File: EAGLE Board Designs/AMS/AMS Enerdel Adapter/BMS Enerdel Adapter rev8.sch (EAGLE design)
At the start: 26 parts, among them J1 CONNECTOR-1_5222_, J10 CONNECTOR-1_5222_, J11 CONNECTOR-1_5222_, J12 CONNECTOR-1_5222_, J13 CONNECTOR-1_5222_, J14 CONNECTOR-1_5222_, J15 CONNECTOR-1_5222_, J16 CONNECTOR-1_5222_, J17 CONNECTOR-1_5222_, J18 CONNECTOR-1_5222_, J19 CONNECTOR-1_5222_, J2 CONNECTOR-1_5222_, J20 CONNECTOR-1_5222_, J21 CONNECTOR-1_5222_, J22 CONNECTOR-1_5222_, J3 CONNECTOR-1_5222_, J4 CONNECTOR-1_5222_, J5 CONNECTOR-1_5222_, J6 CONNECTOR-1_5222_, J7 CONNECTOR-1_5222_, J8 CONNECTOR-1_5222_, J9 CONNECTOR-1_5222_

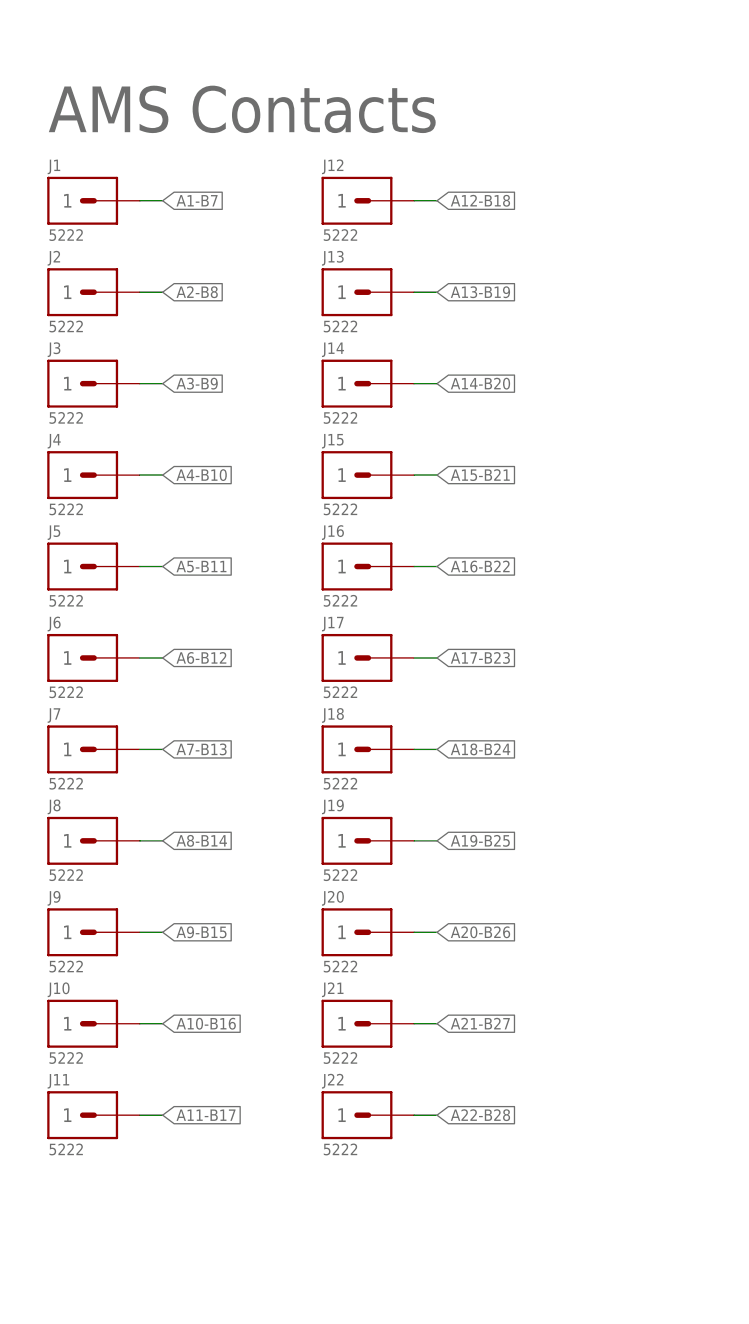
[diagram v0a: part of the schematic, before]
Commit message: added fuses
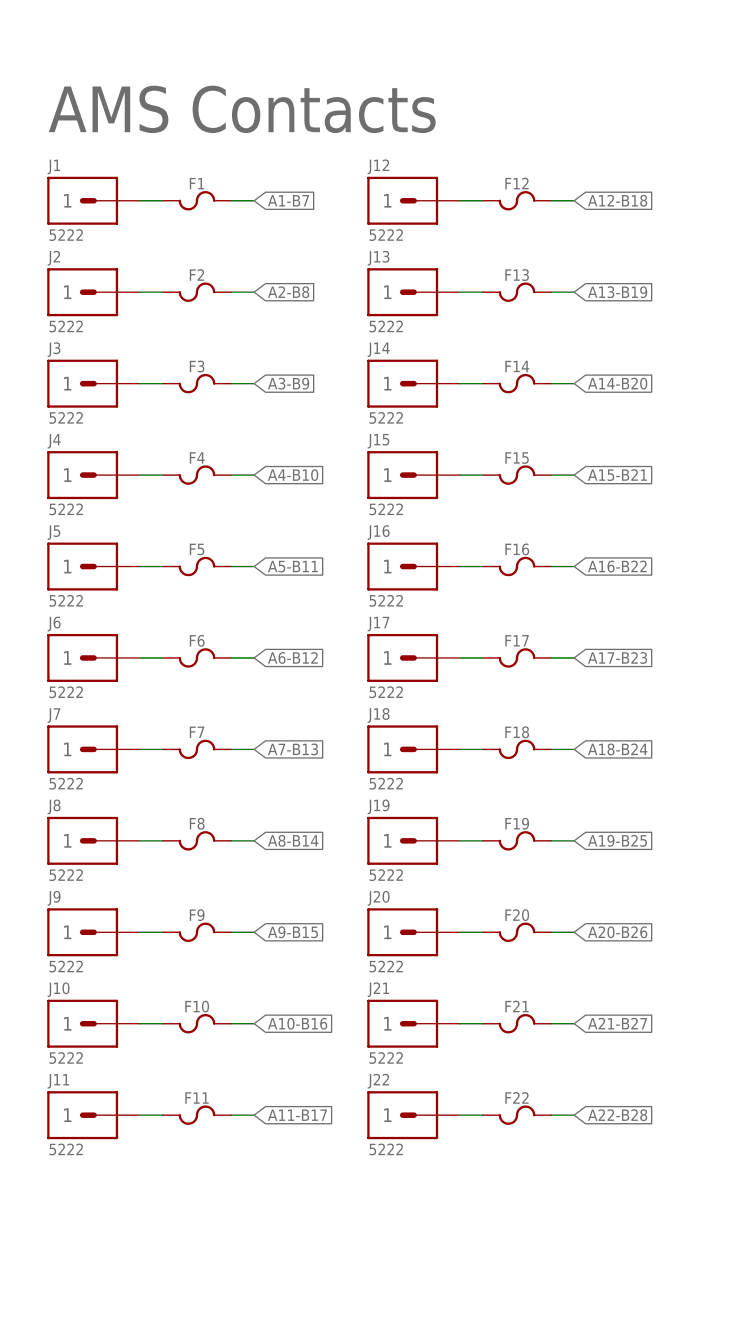
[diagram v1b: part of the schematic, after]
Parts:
- added F1, F10, F11, F12, F13, F14, F15, F16, F17, F18, F19, F2, F20, F21, F22, F3, F4, F5, F6, F7, F8, F9: (no value), HyTechDevices:FUSE_MINIBLADE
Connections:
- new net N$8: F10.1, J10.1
- net A1-B7: now also F1.1, F1.2
- net A10-B16: now also F10.2; no longer J10.1
- net A11-B17: now also F11.1, F11.2
- net A12-B18: now also F12.1, F12.2
- net A13-B19: now also F13.1, F13.2
- net A14-B20: now also F14.1, F14.2
- net A15-B21: now also F15.1, F15.2
- net A16-B22: now also F16.1, F16.2
- net A17-B23: now also F17.1, F17.2
- net A18-B24: now also F18.1, F18.2
- net A19-B25: now also F19.1, F19.2
- net A2-B8: now also F2.1, F2.2
- net A20-B26: now also F20.1, F20.2
- net A21-B27: now also F21.1, F21.2
- net A22-B28: now also F22.1, F22.2
- net A3-B9: now also F3.1, F3.2
- net A4-B10: now also F4.1, F4.2
- net A5-B11: now also F5.1, F5.2
- net A6-B12: now also F6.1, F6.2
- net A7-B13: now also F7.1, F7.2
- net A8-B14: now also F8.1, F8.2
- net A9-B15: now also F9.1, F9.2
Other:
- moved on the sheet: J12, J13, J14, J15, J16, J17, J18, J19, J20, J21, J22

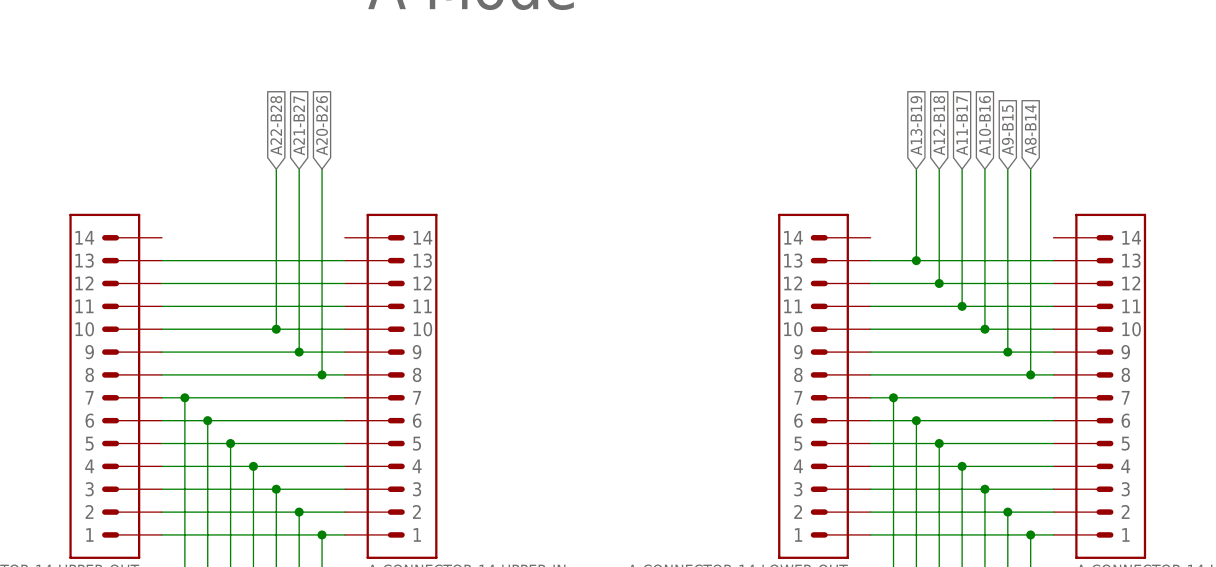
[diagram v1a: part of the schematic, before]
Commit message: routed fuses
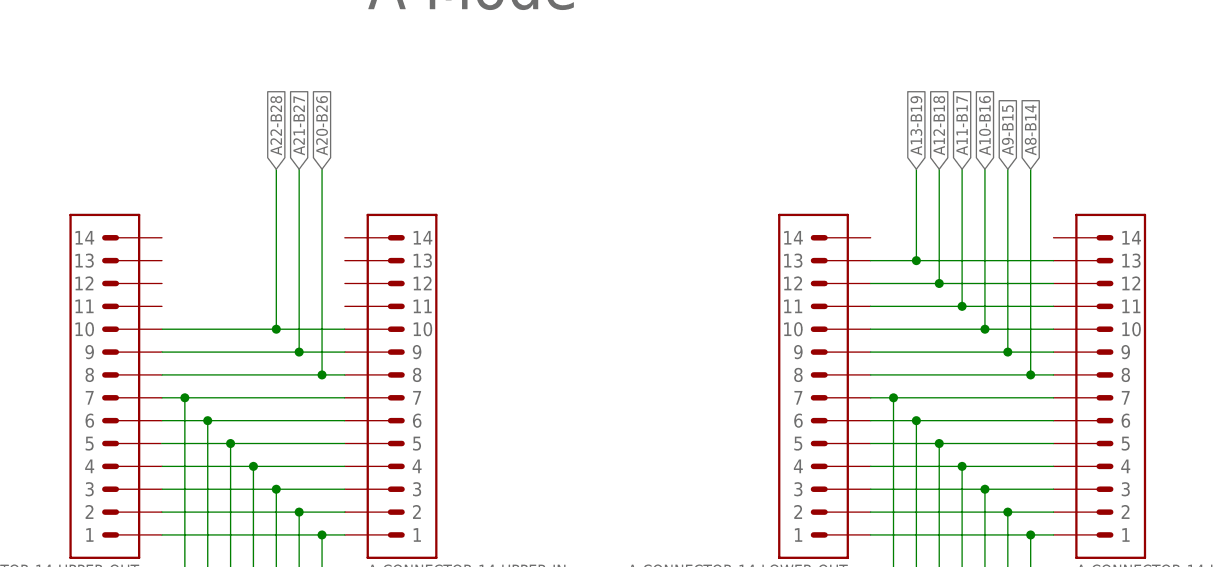
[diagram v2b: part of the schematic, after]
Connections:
- removed net N$5: A-CONNECTOR-14-UPPER-IN.11, A-CONNECTOR-14-UPPER-OUT.11
- removed net N$6: A-CONNECTOR-14-UPPER-IN.12, A-CONNECTOR-14-UPPER-OUT.12
- removed net N$7: A-CONNECTOR-14-UPPER-IN.13, A-CONNECTOR-14-UPPER-OUT.13
- new net N$1: F1.1, J1.1
- new net N$10: F7.1, J7.1
- new net N$11: F8.1, J8.1
- new net N$12: F9.1, J9.1
- new net N$14: F11.1, J11.1
- new net N$15: F22.1, J22.1
- new net N$16: F21.1, J21.1
- new net N$17: F20.1, J20.1
- new net N$18: F19.1, J19.1
- new net N$19: F18.1, J18.1
- new net N$2: F2.1, J2.1
- new net N$20: F17.1, J17.1
- new net N$21: F16.1, J16.1
- new net N$22: F15.1, J15.1
- new net N$23: F14.1, J14.1
- new net N$24: F12.1, J12.1
- new net N$25: F13.1, J13.1
- new net N$3: F3.1, J3.1
- new net N$4: F4.1, J4.1
- new net N$8: F5.1, J5.1
- new net N$9: F6.1, J6.1
- net A1-B7: no longer F1.1, J1.1
- net A11-B17: no longer F11.1, J11.1
- net A12-B18: no longer F12.1, J12.1
- net A13-B19: no longer F13.1, J13.1
- net A14-B20: no longer F14.1, J14.1
- net A15-B21: no longer F15.1, J15.1
- net A16-B22: no longer F16.1, J16.1
- net A17-B23: no longer F17.1, J17.1
- net A18-B24: no longer F18.1, J18.1
- net A19-B25: no longer F19.1, J19.1
- net A2-B8: no longer F2.1, J2.1
- net A20-B26: no longer F20.1, J20.1
- net A21-B27: no longer F21.1, J21.1
- net A22-B28: no longer F22.1, J22.1
- net A3-B9: no longer F3.1, J3.1
- net A4-B10: no longer F4.1, J4.1
- net A5-B11: no longer F5.1, J5.1
- net A6-B12: no longer F6.1, J6.1
- net A7-B13: no longer F7.1, J7.1
- net A8-B14: no longer F8.1, J8.1
- net A9-B15: no longer F9.1, J9.1

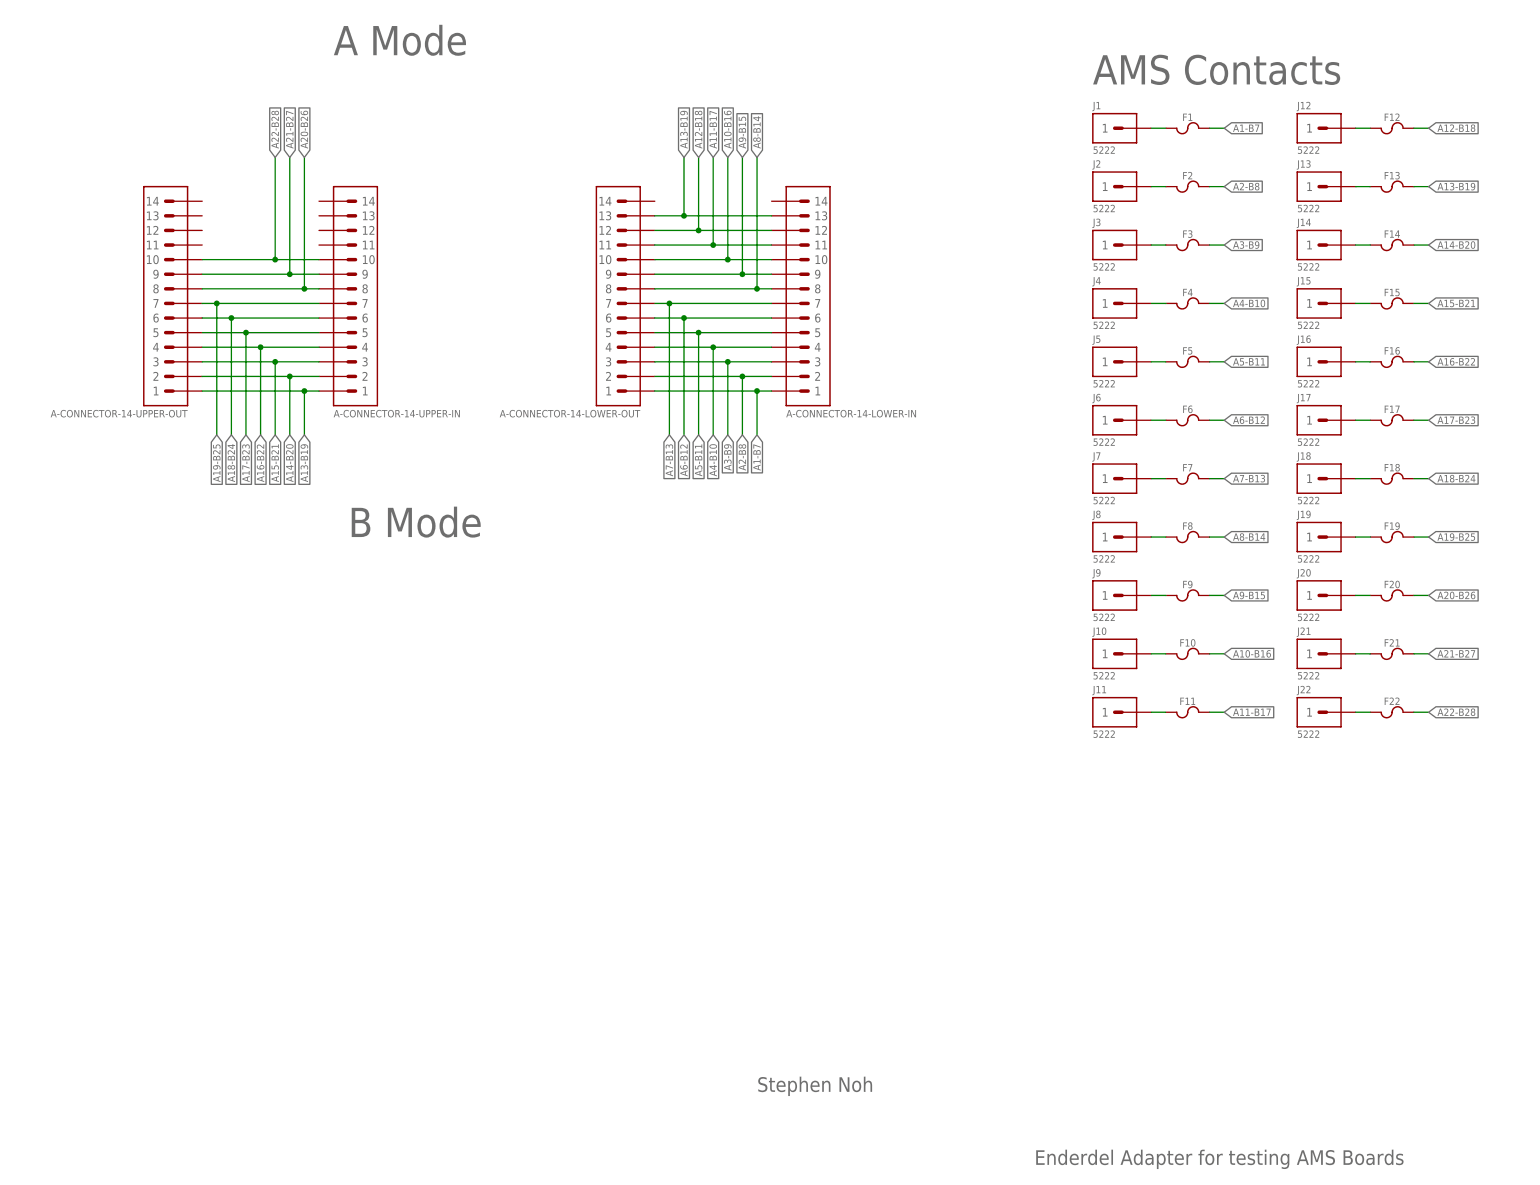
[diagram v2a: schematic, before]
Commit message: fixed fuses and silk screen
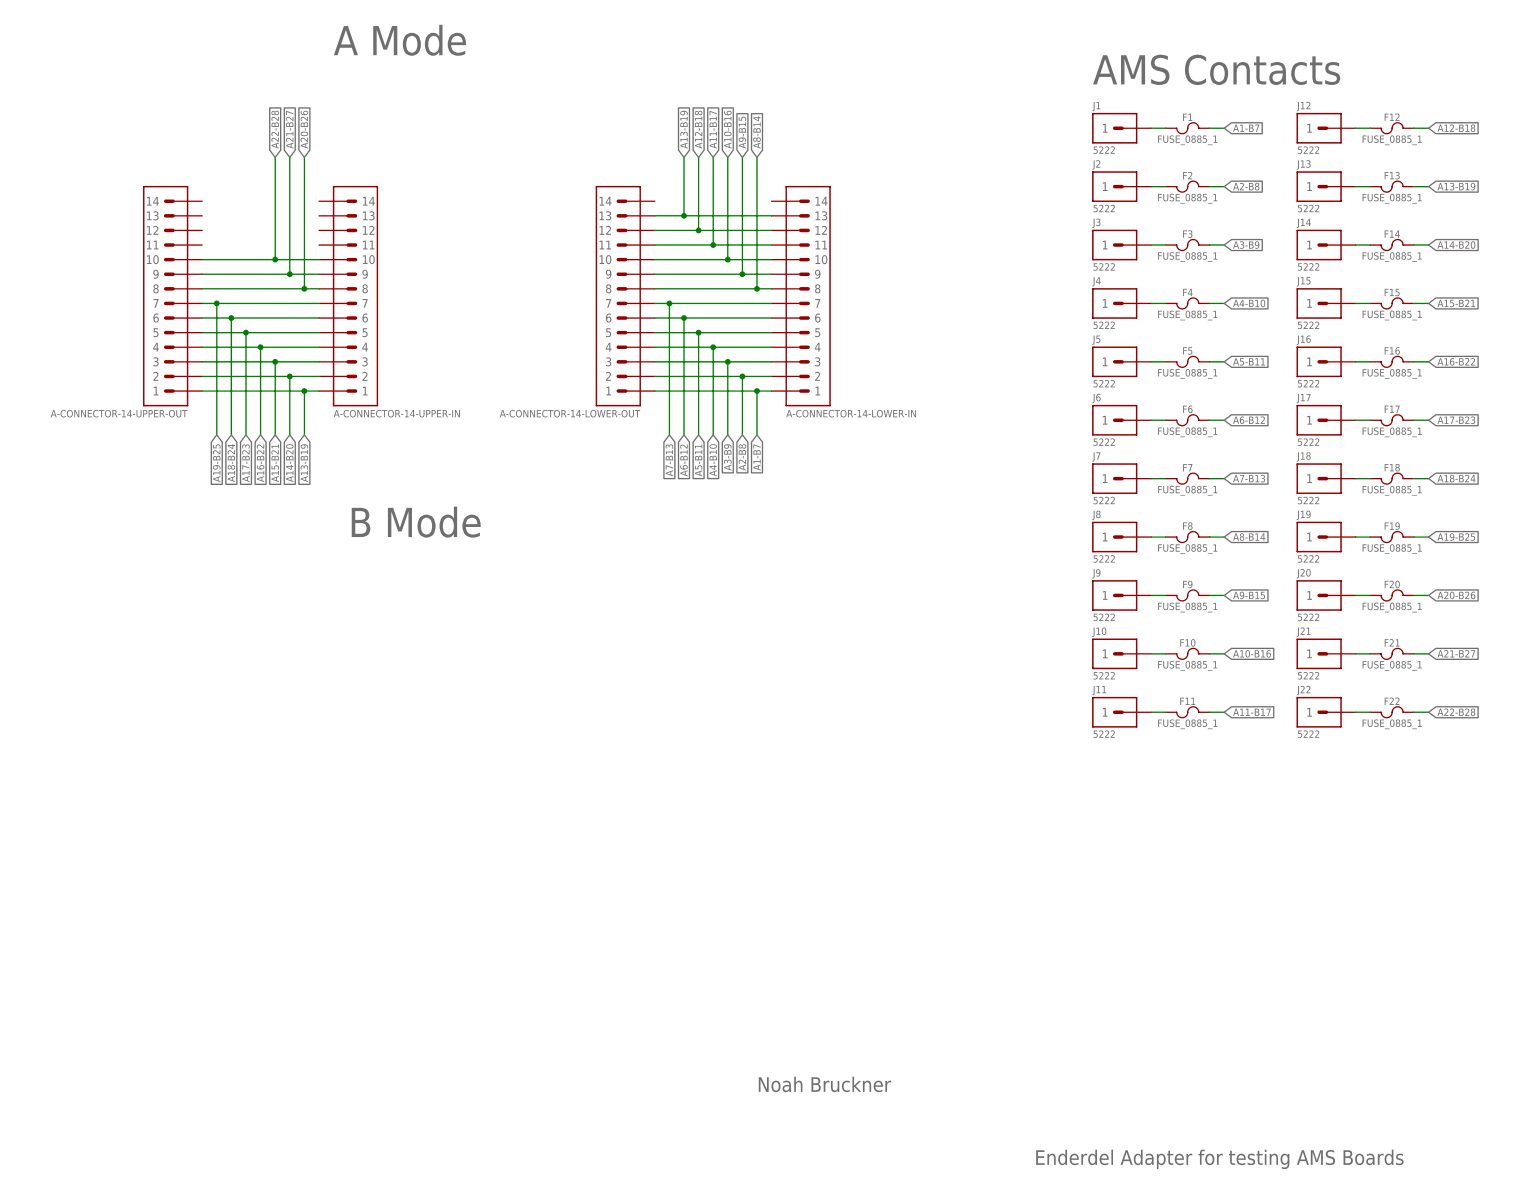
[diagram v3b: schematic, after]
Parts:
- F1, F10, F11, F12, F13, F14, F15, F16, F17, F18, F19, F2, F20, F21, F22, F3, F4, F5, F6, F7, F8, F9: value (none) -> FUSE_0885_1; device HyTechDevices:FUSE_MINIBLADE -> HyTechDevices:FUSE_0885_1
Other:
- note added: "Noah Bruckner"
- note removed: "Stephen Noh"
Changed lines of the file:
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@@
 <drawing>
 <settings>
-<setting alwaysvectorfont="no"/>
+<setting alwaysvectorfont="yes"/>
 <setting verticaltext="up"/>
 </settings>
@@
 <part name="A-CONNECTOR-14-UPPER-IN" library="HyTechDevices" deviceset="CONNECTOR-14_?_*" device="NANOFIT"/>
 <part name="A-CONNECTOR-14-UPPER-OUT" library="HyTechDevices" deviceset="CONNECTOR-14_?_*" device="NANOFIT"/>
-<part name="F1" library="HyTechDevices" deviceset="FUSE" device="_MINIBLADE"/>
-<part name="F2" library="HyTechDevices" deviceset="FUSE" device="_MINIBLADE"/>
-<part name="F3" library="HyTechDevices" deviceset="FUSE" device="_MINIBLADE"/>
-<part name="F4" library="HyTechDevices" deviceset="FUSE" device="_MINIBLADE"/>
-<part name="F5" library="HyTechDevices" deviceset="FUSE" device="_MINIBLADE"/>
-<part name="F6" library="HyTechDevices" deviceset="FUSE" device="_MINIBLADE"/>
-<part name="F7" library="HyTechDevices" deviceset="FUSE" device="_MINIBLADE"/>
-<part name="F8" library="HyTechDevices" deviceset="FUSE" device="_MINIBLADE"/>
-<part name="F9" library="HyTechDevices" deviceset="FUSE" device="_MINIBLADE"/>
-<part name="F10" library="HyTechDevices" deviceset="FUSE" device="_MINIBLADE"/>
-<part name="F11" library="HyTechDevices" deviceset="FUSE" device="_MINIBLADE"/>
-<part name="F12" library="HyTechDevices" deviceset="FUSE" device="_MINIBLADE"/>
-<part name="F13" library="HyTechDevices" deviceset="FUSE" device="_MINIBLADE"/>
-<part name="F14" library="HyTechDevices" deviceset="FUSE" device="_MINIBLADE"/>
-<part name="F15" library="HyTechDevices" deviceset="FUSE" device="_MINIBLADE"/>
-<part name="F16" library="HyTechDevices" deviceset="FUSE" device="_MINIBLADE"/>
-<part name="F17" library="HyTechDevices" deviceset="FUSE" device="_MINIBLADE"/>
-<part name="F18" library="HyTechDevices" deviceset="FUSE" device="_MINIBLADE"/>
-<part name="F19" library="HyTechDevices" deviceset="FUSE" device="_MINIBLADE"/>
-<part name="F20" library="HyTechDevices" deviceset="FUSE" device="_MINIBLADE"/>
-<part name="F21" library="HyTechDevices" deviceset="FUSE" device="_MINIBLADE"/>
-<part name="F22" library="HyTechDevices" deviceset="FUSE" device="_MINIBLADE"/>
+<part name="F1" library="HyTechDevices" deviceset="FUSE_?_*" device="0885" technology="1"/>
+<part name="F2" library="HyTechDevices" deviceset="FUSE_?_*" device="0885" technology="1"/>
+<part name="F3" library="HyTechDevices" deviceset="FUSE_?_*" device="0885" technology="1"/>
+<part name="F4" library="HyTechDevices" deviceset="FUSE_?_*" device="0885" technology="1"/>
+<part name="F5" library="HyTechDevices" deviceset="FUSE_?_*" device="0885" technology="1"/>
+<part name="F6" library="HyTechDevices" deviceset="FUSE_?_*" device="0885" technology="1"/>
+<part name="F7" library="HyTechDevices" deviceset="FUSE_?_*" device="0885" technology="1"/>
+<part name="F8" library="HyTechDevices" deviceset="FUSE_?_*" device="0885" technology="1"/>
+<part name="F9" library="HyTechDevices" deviceset="FUSE_?_*" device="0885" technology="1"/>
+<part name="F10" library="HyTechDevices" deviceset="FUSE_?_*" device="0885" technology="1"/>
+<part name="F11" library="HyTechDevices" deviceset="FUSE_?_*" device="0885" technology="1"/>
+<part name="F12" library="HyTechDevices" deviceset="FUSE_?_*" device="0885" technology="1"/>
+<part name="F13" library="HyTechDevices" deviceset="FUSE_?_*" device="0885" technology="1"/>
+<part name="F14" library="HyTechDevices" deviceset="FUSE_?_*" device="0885" technology="1"/>
+<part name="F15" library="HyTechDevices" deviceset="FUSE_?_*" device="0885" technology="1"/>
+<part name="F16" library="HyTechDevices" deviceset="FUSE_?_*" device="0885" technology="1"/>
+<part name="F17" library="HyTechDevices" deviceset="FUSE_?_*" device="0885" technology="1"/>
+<part name="F18" library="HyTechDevices" deviceset="FUSE_?_*" device="0885" technology="1"/>
+<part name="F19" library="HyTechDevices" deviceset="FUSE_?_*" device="0885" technology="1"/>
+<part name="F20" library="HyTechDevices" deviceset="FUSE_?_*" device="0885" technology="1"/>
+<part name="F21" library="HyTechDevices" deviceset="FUSE_?_*" device="0885" technology="1"/>
+<part name="F22" library="HyTechDevices" deviceset="FUSE_?_*" device="0885" technology="1"/>
 </parts>
 <sheets>
 <sheet>
 <plain>
-<text x="129.54" y="22.86" size="2.54" layer="95">Stephen Noh</text>
+<text x="129.54" y="22.86" size="2.54" layer="95">Noah Bruckner</text>
 <text x="187.96" y="198.12" size="5.08" layer="95">AMS Contacts</text>
 <text x="55.88" y="203.2" size="5.08" layer="95">A Mode</text>
@@
 </schematic>
 </drawing>
-<compatibility>
-<note version="6.3" minversion="6.2.2" severity="warning">
-Since Version 6.2.2 text objects can contain more than one line,
-which will not be processed correctly with this version.
-</note>
-</compatibility>
 </eagle>
